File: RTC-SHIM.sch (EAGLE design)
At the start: 15 parts, among them IC1 DS3231/SO

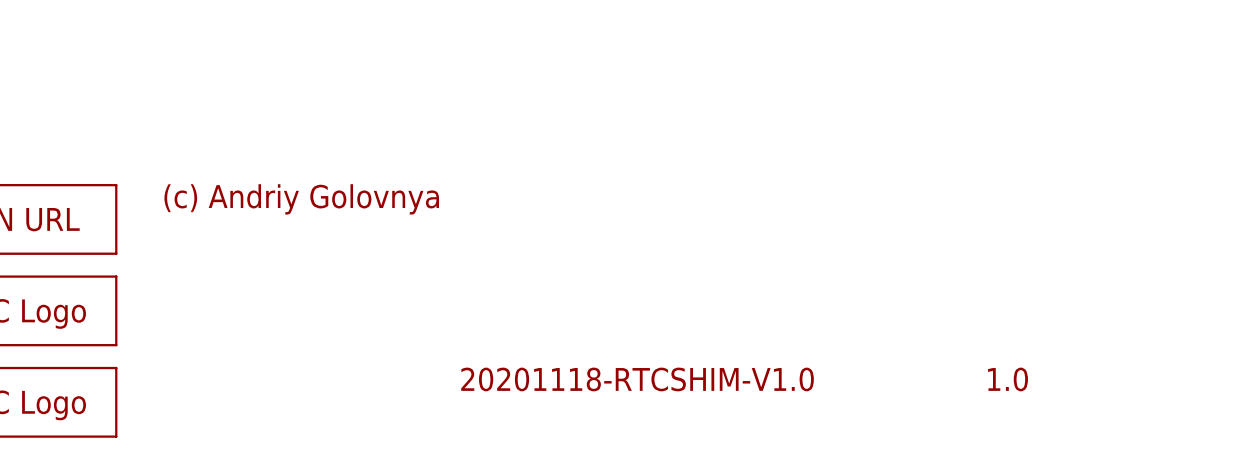
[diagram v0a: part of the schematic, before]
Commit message: Add few texts. Move some traces around. Updated description.
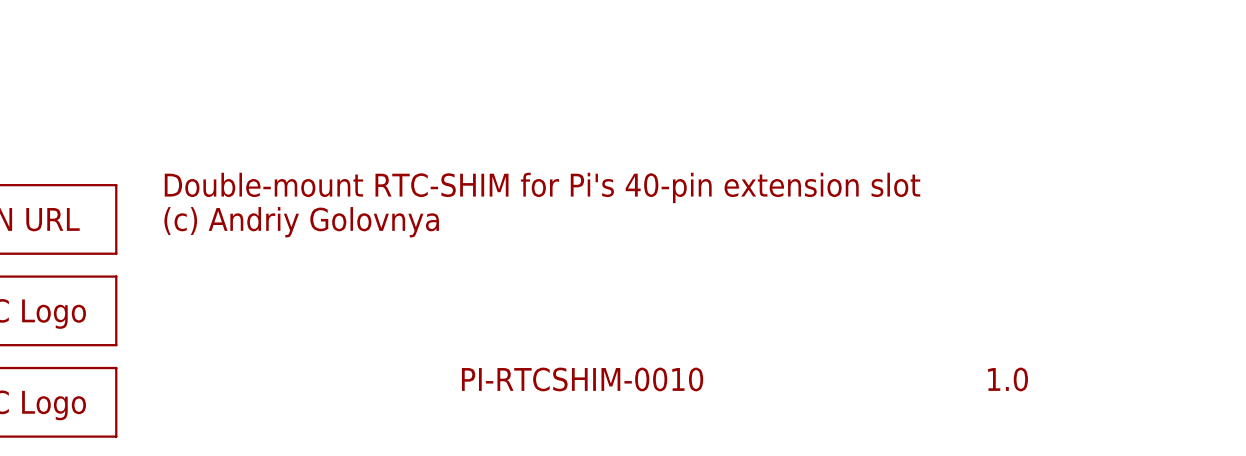
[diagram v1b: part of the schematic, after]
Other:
- note added: "Double-mount RTC-SHIM for Pi's 40-pin extension slot (c) Andriy Golovnya"
- note added: "PI-RTCSHIM-0010"
- note removed: "(c) Andriy Golovnya"
- note removed: "20201118-RTCSHIM-V1.0"
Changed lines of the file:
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@@
 <plain>
 <text x="256.54" y="7.62" size="2.54" layer="94">1.0</text>
-<text x="198.12" y="7.62" size="2.54" layer="94">20201118-RTCSHIM-V1.0</text>
-<text x="165.1" y="27.94" size="2.54" layer="94">(c) Andriy Golovnya</text>
+<text x="198.12" y="7.62" size="2.54" layer="94">PI-RTCSHIM-0010</text>
+<text x="165.1" y="25.4" size="2.54" layer="94">Double-mount RTC-SHIM for Pi's 40-pin extension slot
+(c) Andriy Golovnya</text>
 <text x="43.18" y="139.7" size="2.54" layer="94">RTC chip</text>
 <text x="38.1" y="81.28" size="2.54" layer="94">Caps and pullups</text>

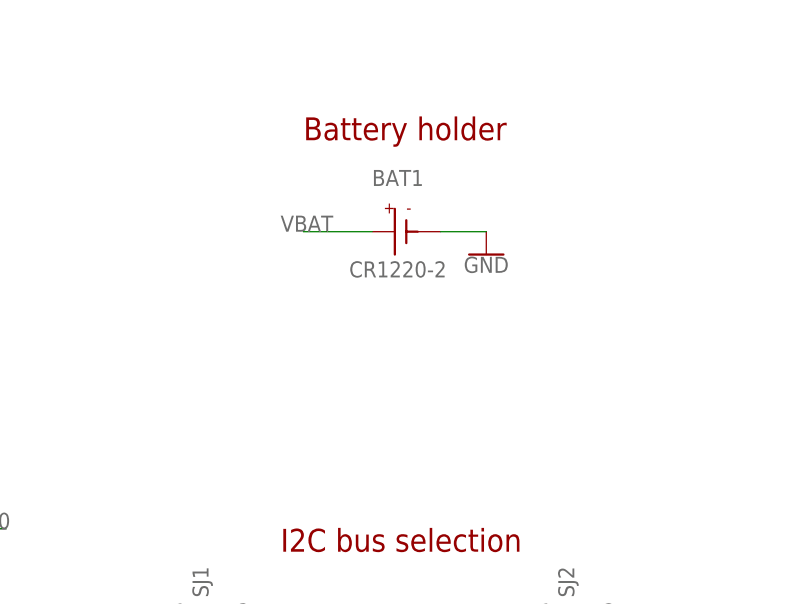
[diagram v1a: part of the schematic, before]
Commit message: Added battery connector. Generated CAM.
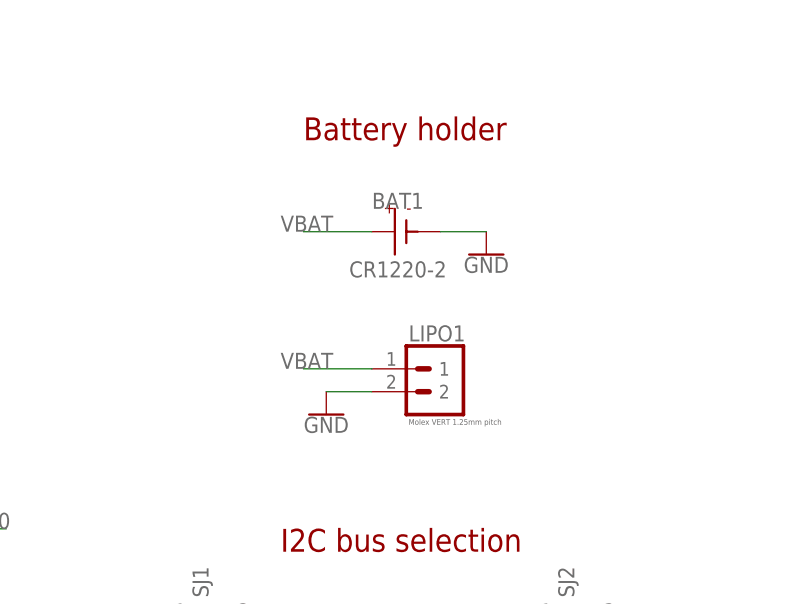
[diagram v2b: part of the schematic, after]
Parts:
- added LIPO1: Molex VERT 1.25mm pitch, PiB_connectors:1X02_MOLEX_0530470210_VERT-MALE_PITCH-1.25MM
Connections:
- net GND: now also LIPO1.2
- net VBAT: now also LIPO1.1
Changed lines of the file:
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@@
 <layer number="154" name="FabDoc2" color="2" fill="1" visible="no" active="no"/>
 <layer number="155" name="FabDoc3" color="7" fill="15" visible="no" active="no"/>
+<layer number="160" name="tMountFaceplate" color="7" fill="1" visible="yes" active="yes"/>
+<layer number="161" name="bMountFaceplate" color="7" fill="1" visible="yes" active="yes"/>
+<layer number="162" name="tCopperArt" color="7" fill="1" visible="yes" active="yes"/>
+<layer number="163" name="bCopperArt" color="7" fill="1" visible="yes" active="yes"/>
+<layer number="164" name="tRubout" color="7" fill="1" visible="yes" active="yes"/>
+<layer number="165" name="bRubout" color="7" fill="1" visible="yes" active="yes"/>
+<layer number="167" name="Fiducials" color="7" fill="1" visible="yes" active="yes"/>
+<layer number="169" name="internal" color="7" fill="1" visible="yes" active="yes"/>
 <layer number="199" name="Contour" color="7" fill="1" visible="no" active="yes"/>
 <layer number="200" name="200bmp" color="1" fill="10" visible="no" active="yes"/>
@@
 <part name="LOGO2" library="_my_logos" deviceset="MFDECLOGO" device="_L_20MM" value="MFDECLOGO_L_20MM"/>
 <part name="LOGO3" library="_my_logos" deviceset="RSNURL" device="_QR_10MM"/>
+<part name="LIPO1" library="PiB_connectors" deviceset="1X02_MOLEX" device="_0530470210_VERT-MALE_PITCH-1.25MM" package3d_urn="urn:adsk.eagle:package:2973718/3" value="Molex VERT 1.25mm pitch"/>
+<part name="GND11" library="SparkFun-PowerSymbols" library_urn="urn:adsk.eagle:library:530" deviceset="GND" device=""/>
 </parts>
 <sheets>
@@
 </instance>
 <instance part="BAT1" gate="G$1" x="220.98" y="116.84" smashed="yes">
-<attribute name="NAME" x="218.44" y="121.92" size="1.778" layer="96"/>
+<attribute name="NAME" x="218.44" y="119.38" size="1.778" layer="96"/>
 <attribute name="VALUE" x="215.9" y="111.76" size="1.778" layer="96"/>
 </instance>
@@
 <instance part="LOGO2" gate="G$1" x="134.62" y="12.7" smashed="yes"/>
 <instance part="LOGO3" gate="G$1" x="139.7" y="22.86" smashed="yes"/>
+<instance part="LIPO1" gate="G$1" x="226.06" y="101.6" smashed="yes" rot="MR0">
+<attribute name="VALUE" x="222.504" y="96.012" size="0.635" layer="96" font="vector" ratio="10" rot="MR0" align="top-right"/>
+<attribute name="NAME" x="222.504" y="104.648" size="1.778" layer="95" ratio="10" rot="MR0" align="bottom-right"/>
+</instance>
+<instance part="GND11" gate="1" x="213.36" y="96.52" smashed="yes">
+<attribute name="VALUE" x="213.36" y="96.266" size="1.778" layer="96" align="top-center"/>
+</instance>
 </instances>
 <busses>
@@
 <wire x1="218.44" y1="116.84" x2="210.82" y2="116.84" width="0.1524" layer="91"/>
 <label x="208.28" y="116.84" size="1.778" layer="95"/>
+</segment>
+<segment>
+<pinref part="LIPO1" gate="G$1" pin="1"/>
+<wire x1="218.44" y1="101.6" x2="210.82" y2="101.6" width="0.1524" layer="91"/>
+<label x="208.28" y="101.6" size="1.778" layer="95"/>
 </segment>
 </net>
@@
 <pinref part="GND9" gate="1" pin="GND"/>
 </segment>
+<segment>
+<pinref part="LIPO1" gate="G$1" pin="2"/>
+<wire x1="218.44" y1="99.06" x2="213.36" y2="99.06" width="0.1524" layer="91"/>
+<pinref part="GND11" gate="1" pin="GND"/>
+</segment>
 </net>

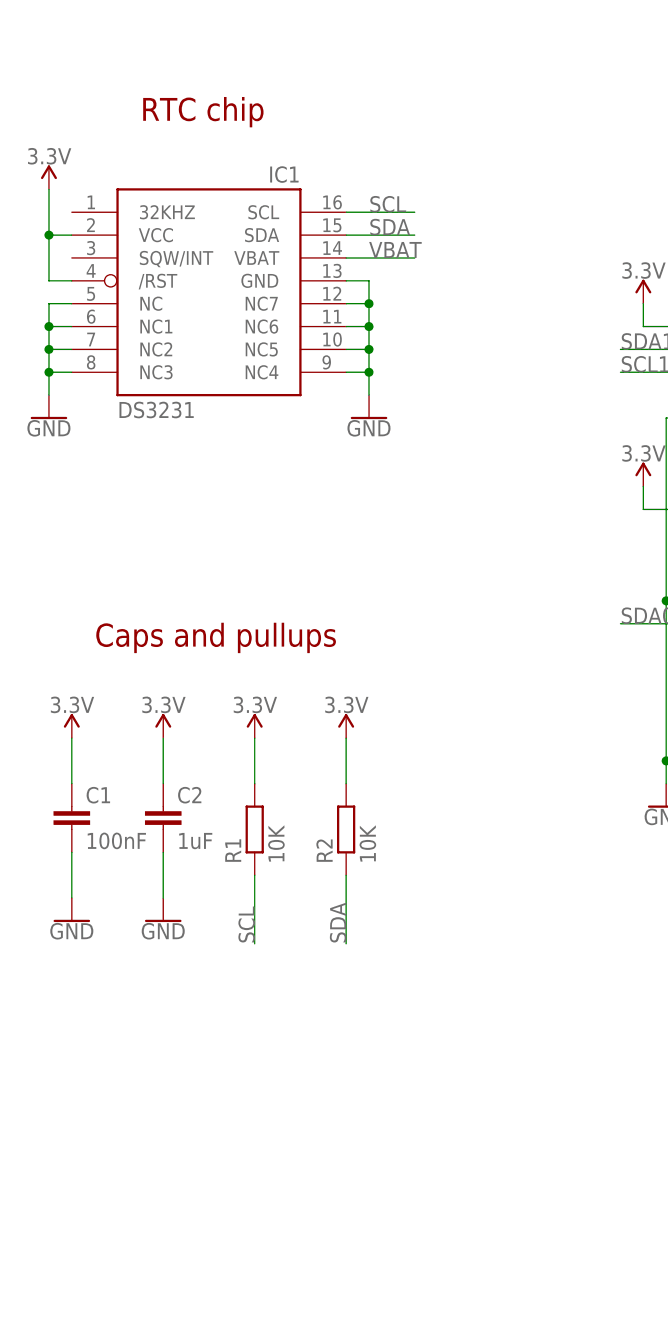
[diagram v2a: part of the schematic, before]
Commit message: Moved some stuff around. Add second footprint. Moved battery away from center for better flipability.
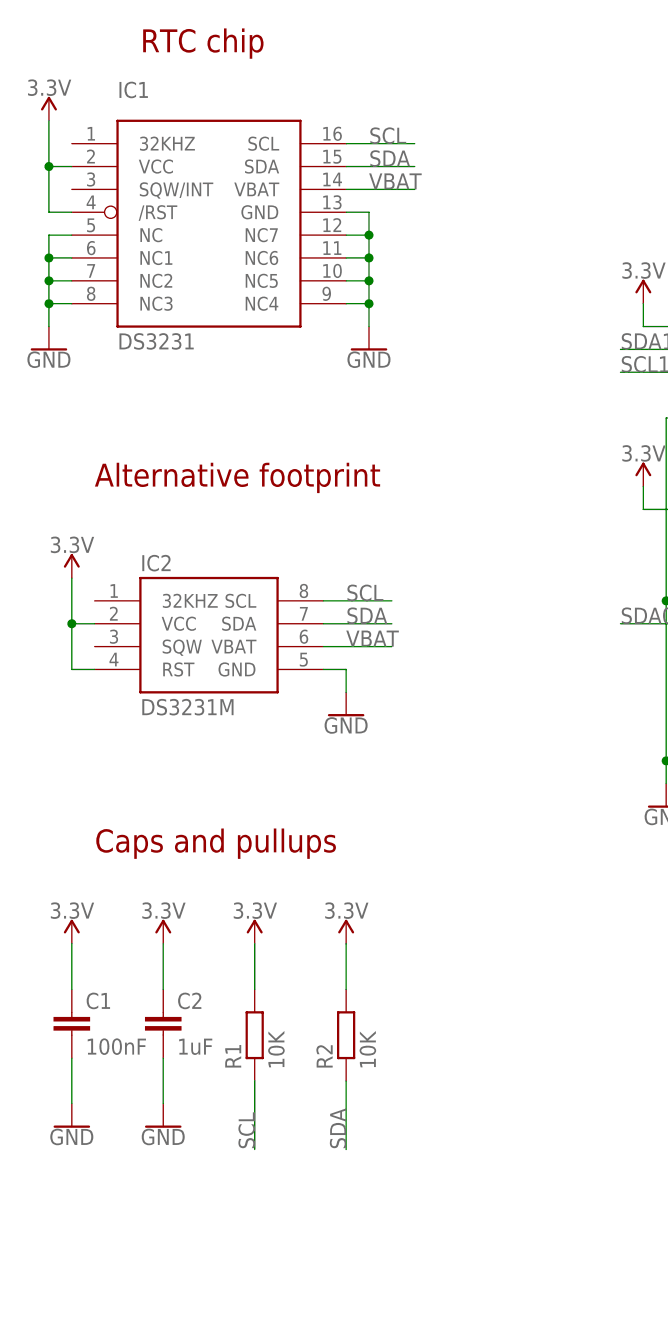
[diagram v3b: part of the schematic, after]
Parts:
- added IC2: DS3231M, SparkFun-Clocks:DS3231M
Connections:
- net 3.3V: now also IC2.RST, IC2.VCC
- net GND: now also IC2.GND
- net SCL: now also IC2.SCL
- net SDA: now also IC2.SDA
- net VBAT: now also IC2.VBAT
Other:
- note added: "Alternative footprint"
- moved on the sheet: C1, C2, IC1, R1, R2
